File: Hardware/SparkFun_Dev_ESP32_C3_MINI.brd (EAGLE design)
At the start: 17.8 x 33 mm, 44 parts, among them J1 USB Female Type C Connector, J5 Vertical Qwiic Connector, U2 RT9080-33GJ5

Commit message: Some updates to layout
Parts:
- moved U$1 5.46 mm to (10.2, 11.2)
- moved J5 4.57 mm to (10.2, 21.1)
- moved C8 3.81 mm to (17.8, 6.35)
- moved C9 3.43 mm to (17.8, 7.24)
- moved R3 2.54 mm to (15.2, 17.8)
- moved R4 2.54 mm to (5.08, 17.8)
- moved C1 2.54 mm to (12.7, 24.1)
- moved C2 2.54 mm to (12.7, 22.9)
- moved C5 2.54 mm to (7.62, 22.9)
- moved R11 2.54 mm to (7.62, 24.1)
- moved R5 2.54 mm to (7.62, 25.4)
- moved R6 2.54 mm to (12.7, 25.4)
- moved U2 1.65 mm to (10.2, 23.2)
- moved BOOT 1.27 mm to (15.2, 22.9)
- moved R7 1.27 mm to (5.08, 19.1)
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
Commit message: Removes unnecessary documents, , moves boar daround
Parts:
- moved PWR 16.7 mm to (6.22, 15.2)
- moved STAT 16.7 mm to (14.6, 15.2)
- moved FD3 15.3 mm to (2.54, 6.35)
- moved FD4 15.3 mm to (2.54, 6.35)
- moved LOGO2 12.3 mm to (14.2, 18.5), turned to 90 degrees
- moved FD1 10.2 mm to (16.5, 26.7), flipped to the bottom
- moved FD2 10.2 mm to (16.5, 26.7), flipped to the top
- moved SHLD 5.36 mm to (14.7, 29.8), turned to 0 degrees
- moved R9 1.27 mm to (16.5, 19.1), turned to 90 degrees
- moved TP1 1.27 mm to (15.2, 12.7)
- moved TP6 1.27 mm to (12.7, 12.7)
- moved TP3 1.27 mm to (15.2, 7.62)
- moved TP4 1.27 mm to (12.7, 7.62)
- moved R3 1.27 mm to (15.2, 19.1), turned to 90 degrees
- moved TP2 1.27 mm to (15.2, 10.2)
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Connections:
- net IO10: now also U$2.2, U$2.2B; no longer U$2.1, U$2.1B
- net IO8: now also U$2.1, U$2.1B; no longer U$2.2, U$2.2B
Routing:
- added copper zone on layer 15, net 3V3
- added copper zone on layer 1, net GND
- added copper zone on layer 16, net GND
- added copper zone on layer 2, net GND

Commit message: Fixes net names that were blasted away
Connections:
- removed net IO7/STAT: STAT.2, TP1.1, U$1.21, U$2.3, U$2.3B
- removed net IOA0/SCLK: U$1.12, U$3.7, U$3.7B
- removed net IOA1/POCI: U$1.13, U$3.6, U$3.6B
- removed net IOA3/PICO: TP4.1, U$1.6, U$3.5, U$3.5B
- removed net IOA4: U$1.18, U$3.8, U$3.8B
- new net IO7: U$1.21, U$2.3, U$2.3B
- new net IOA0/SCLK/MTCK: TP3.1, U$1.12, U$3.7, U$3.7B
- new net IOA1/POCI/MTDO: STAT.2, TP1.1, U$1.13, U$3.6, U$3.6B
- new net IOA3/PICO/MTDI: TP6.1, U$1.6, U$3.5, U$3.5B
- new net IOA4/MTMS: TP4.1, U$1.18, U$3.8, U$3.8B
- net IO5/SCL: no longer TP6.1
- net IO6/SDA: no longer TP3.1
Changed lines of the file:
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@@
 <wire x1="19.35" y1="8.89" x2="17.78" y2="8.89" width="0" layer="19" extent="1-1"/>
 </signal>
-<signal name="IO7/STAT">
-<contactref element="TP1" pad="1"/>
-<contactref element="U$1" pad="21"/>
-<contactref element="STAT" pad="2"/>
-<contactref element="U$2" pad="3B"/>
-<contactref element="U$2" pad="3"/>
-<wire x1="15.1257" y1="15.24" x2="15.24" y2="12.7" width="0" layer="19" extent="16-16"/>
-<wire x1="7.76" y1="16.076" x2="15.1257" y2="15.24" width="0" layer="19" extent="1-16"/>
-<wire x1="2.54" y1="13.97" x2="7.76" y2="16.076" width="0" layer="19" extent="1-1"/>
-<wire x1="0.97" y1="13.97" x2="2.54" y2="13.97" width="0" layer="19" extent="1-1"/>
-</signal>
-<signal name="IOA3/PICO">
-<contactref element="TP4" pad="1"/>
+<signal name="IOA3/PICO/MTDI">
 <contactref element="U$1" pad="6"/>
 <contactref element="U$3" pad="5"/>
 <contactref element="U$3" pad="5B"/>
+<contactref element="TP6" pad="1"/>
 <wire x1="19.35" y1="19.05" x2="17.78" y2="19.05" width="0" layer="19" extent="1-1"/>
 <wire x1="16.06" y1="11.176" x2="17.78" y2="19.05" width="0" layer="19" extent="1-1"/>
-<wire x1="12.7" y1="7.62" x2="16.06" y2="11.176" width="0" layer="19" extent="1-16"/>
+<wire x1="12.7" y1="12.7" x2="16.06" y2="11.176" width="0" layer="19" extent="1-16"/>
 </signal>
-<signal name="IOA1/POCI">
+<signal name="IOA1/POCI/MTDO">
 <contactref element="U$1" pad="13"/>
 <contactref element="U$3" pad="6"/>
 <contactref element="U$3" pad="6B"/>
+<contactref element="TP1" pad="1"/>
+<contactref element="STAT" pad="2"/>
 <wire x1="19.35" y1="16.51" x2="17.78" y2="16.51" width="0" layer="19" extent="1-1"/>
-<wire x1="14.16" y1="16.076" x2="17.78" y2="16.51" width="0" layer="19" extent="1-1"/>
+<wire x1="15.1257" y1="15.24" x2="17.78" y2="16.51" width="0" layer="19" extent="16-16"/>
+<wire x1="14.16" y1="16.076" x2="15.1257" y2="15.24" width="0" layer="19" extent="1-16"/>
+<wire x1="15.24" y1="12.7" x2="15.1257" y2="15.24" width="0" layer="19" extent="16-16"/>
 </signal>
-<signal name="IOA0/SCLK">
+<signal name="IOA0/SCLK/MTCK">
 <contactref element="U$1" pad="12"/>
 <contactref element="U$3" pad="7B"/>
 <contactref element="U$3" pad="7"/>
+<contactref element="TP3" pad="1"/>
 <wire x1="17.78" y1="13.97" x2="19.35" y2="13.97" width="0" layer="19" extent="1-1"/>
 <wire x1="14.96" y1="16.076" x2="17.78" y2="13.97" width="0" layer="19" extent="1-1"/>
+<wire x1="15.24" y1="7.62" x2="17.78" y2="13.97" width="0" layer="19" extent="16-16"/>
 </signal>
 <signal name="N$3">
@@
 <wire x1="6.16" y1="16.076" x2="14.44" y2="20.81" width="0" layer="19" extent="1-1"/>
 </signal>
-<signal name="IOA4">
+<signal name="IOA4/MTMS">
 <contactref element="U$1" pad="18"/>
 <contactref element="U$3" pad="8B"/>
 <contactref element="U$3" pad="8"/>
+<contactref element="TP4" pad="1"/>
 <wire x1="17.78" y1="11.43" x2="19.35" y2="11.43" width="0" layer="19" extent="1-1"/>
-<wire x1="10.16" y1="16.076" x2="17.78" y2="11.43" width="0" layer="19" extent="1-1"/>
+<wire x1="12.7" y1="7.62" x2="17.78" y2="11.43" width="0" layer="19" extent="16-16"/>
+<wire x1="10.16" y1="16.076" x2="12.7" y2="7.62" width="0" layer="19" extent="1-16"/>
 </signal>
 <signal name="IO5/SCL">
 <contactref element="J5" pad="4"/>
-<contactref element="TP6" pad="1"/>
 <contactref element="U$1" pad="19"/>
 <contactref element="R4" pad="2"/>
@@
 <wire x1="0.97" y1="19.05" x2="2.54" y2="19.05" width="0" layer="19" extent="1-1"/>
 <wire x1="9.36" y1="16.076" x2="5.58" y2="17.78" width="0" layer="19" extent="1-1"/>
-<wire x1="12.7" y1="12.7" x2="9.36" y2="16.076" width="0" layer="19" extent="1-16"/>
 </signal>
 <signal name="IO6/SDA">
 <contactref element="J5" pad="3"/>
-<contactref element="TP3" pad="1"/>
 <contactref element="U$1" pad="20"/>
 <contactref element="R3" pad="1"/>
@@
 <wire x1="2.54" y1="16.51" x2="8.56" y2="16.076" width="0" layer="19" extent="1-1"/>
 <wire x1="0.97" y1="16.51" x2="2.54" y2="16.51" width="0" layer="19" extent="1-1"/>
-<wire x1="15.24" y1="7.62" x2="8.56" y2="16.076" width="0" layer="19" extent="1-16"/>
 </signal>
 <signal name="3V3">
@@
 </polygon>
 </signal>
+<signal name="IO7">
+<contactref element="U$2" pad="3B"/>
+<contactref element="U$2" pad="3"/>
+<contactref element="U$1" pad="21"/>
+<wire x1="2.54" y1="13.97" x2="7.76" y2="16.076" width="0" layer="19" extent="1-1"/>
+<wire x1="0.97" y1="13.97" x2="2.54" y2="13.97" width="0" layer="19" extent="1-1"/>
+</signal>
 </signals>

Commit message: Adds I2S nets, we'll see
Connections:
- net IO10 renamed IO10/I2S_WS
- net IO5/SCL renamed IO5/SCL/BCK
- net IO6/SDA renamed IO6/SDA/I2S_SDO
- net IO7 renamed IO7/I2S_SDI
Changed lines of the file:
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@@
 <layers>
 <layer number="1" name="Top" color="4" fill="1" visible="yes" active="yes"/>
-<layer number="2" name="Route2" color="23" fill="1" visible="yes" active="yes"/>
-<layer number="15" name="Route15" color="10" fill="1" visible="yes" active="yes"/>
+<layer number="2" name="Route2" color="23" fill="1" visible="no" active="yes"/>
+<layer number="15" name="Route15" color="10" fill="1" visible="no" active="yes"/>
 <layer number="16" name="Bottom" color="3" fill="1" visible="yes" active="yes"/>
 <layer number="17" name="Pads" color="26" fill="1" visible="yes" active="yes"/>
@@
 <layer number="19" name="Unrouted" color="6" fill="1" visible="yes" active="yes"/>
 <layer number="20" name="Dimension" color="15" fill="1" visible="yes" active="yes"/>
-<layer number="21" name="tPlace" color="16" fill="1" visible="no" active="yes"/>
-<layer number="22" name="bPlace" color="14" fill="1" visible="no" active="yes"/>
+<layer number="21" name="tPlace" color="16" fill="1" visible="yes" active="yes"/>
+<layer number="22" name="bPlace" color="14" fill="1" visible="yes" active="yes"/>
 <layer number="23" name="tOrigins" color="15" fill="1" visible="yes" active="yes"/>
 <layer number="24" name="bOrigins" color="15" fill="1" visible="yes" active="yes"/>
@@
 <layer number="37" name="tTest" color="7" fill="1" visible="no" active="yes"/>
 <layer number="38" name="bTest" color="7" fill="1" visible="no" active="yes"/>
-<layer number="39" name="tKeepout" color="4" fill="11" visible="yes" active="yes"/>
+<layer number="39" name="tKeepout" color="4" fill="11" visible="no" active="yes"/>
 <layer number="40" name="bKeepout" color="1" fill="11" visible="no" active="yes"/>
 <layer number="41" name="tRestrict" color="4" fill="10" visible="no" active="yes"/>
@@
 <wire x1="14.0843" y1="15.24" x2="18.264" y2="31.75" width="0" layer="19" extent="1-16"/>
 </signal>
-<signal name="IO10">
+<signal name="IO10/I2S_WS">
 <contactref element="U$1" pad="16"/>
 <contactref element="U$2" pad="2B"/>
@@
 <wire x1="10.16" y1="16.076" x2="12.7" y2="7.62" width="0" layer="19" extent="1-16"/>
 </signal>
-<signal name="IO5/SCL">
+<signal name="IO5/SCL/BCK">
 <contactref element="J5" pad="4"/>
 <contactref element="U$1" pad="19"/>
@@
 <wire x1="9.36" y1="16.076" x2="5.58" y2="17.78" width="0" layer="19" extent="1-1"/>
 </signal>
-<signal name="IO6/SDA">
+<signal name="IO6/SDA/I2S_SDO">
 <contactref element="J5" pad="3"/>
 <contactref element="U$1" pad="20"/>
@@
 </polygon>
 </signal>
-<signal name="IO7">
+<signal name="IO7/I2S_SDI">
 <contactref element="U$2" pad="3B"/>
 <contactref element="U$2" pad="3"/>

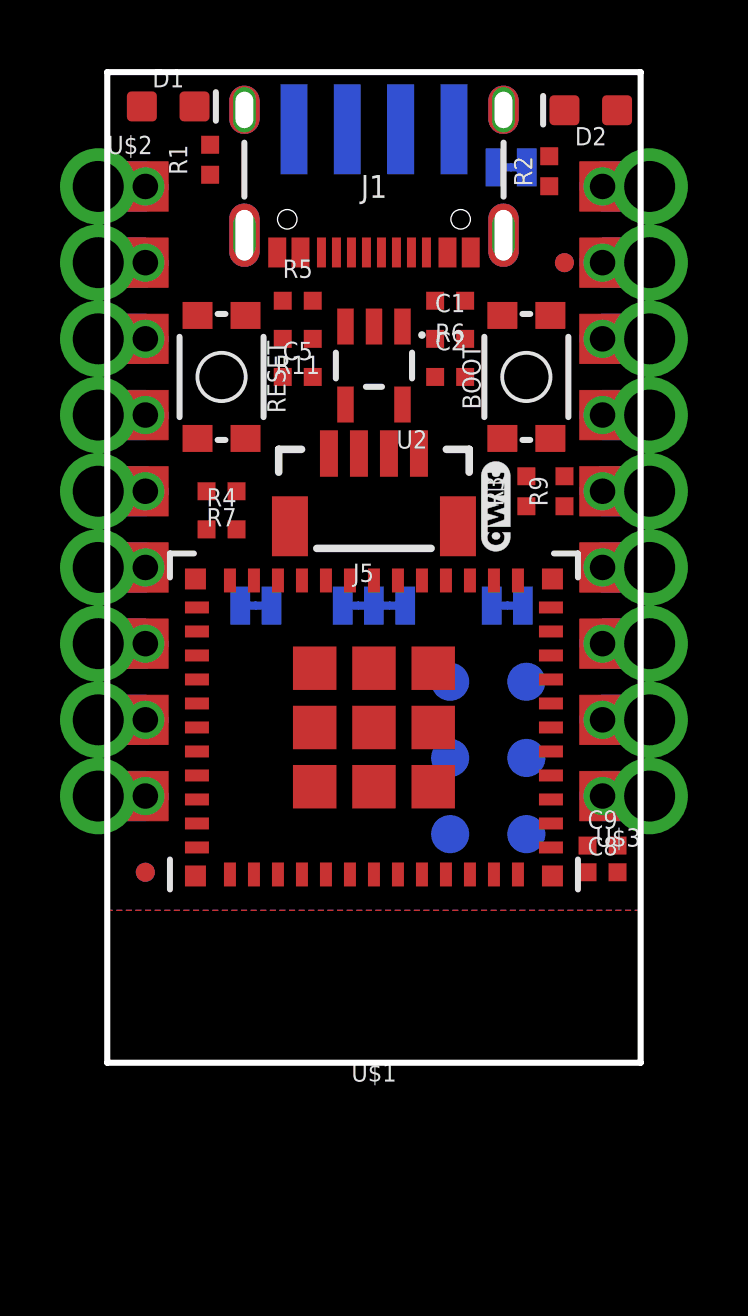
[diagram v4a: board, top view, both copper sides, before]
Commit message: Adds new C3 module so that the  device value is correct
* Fixes testpoints
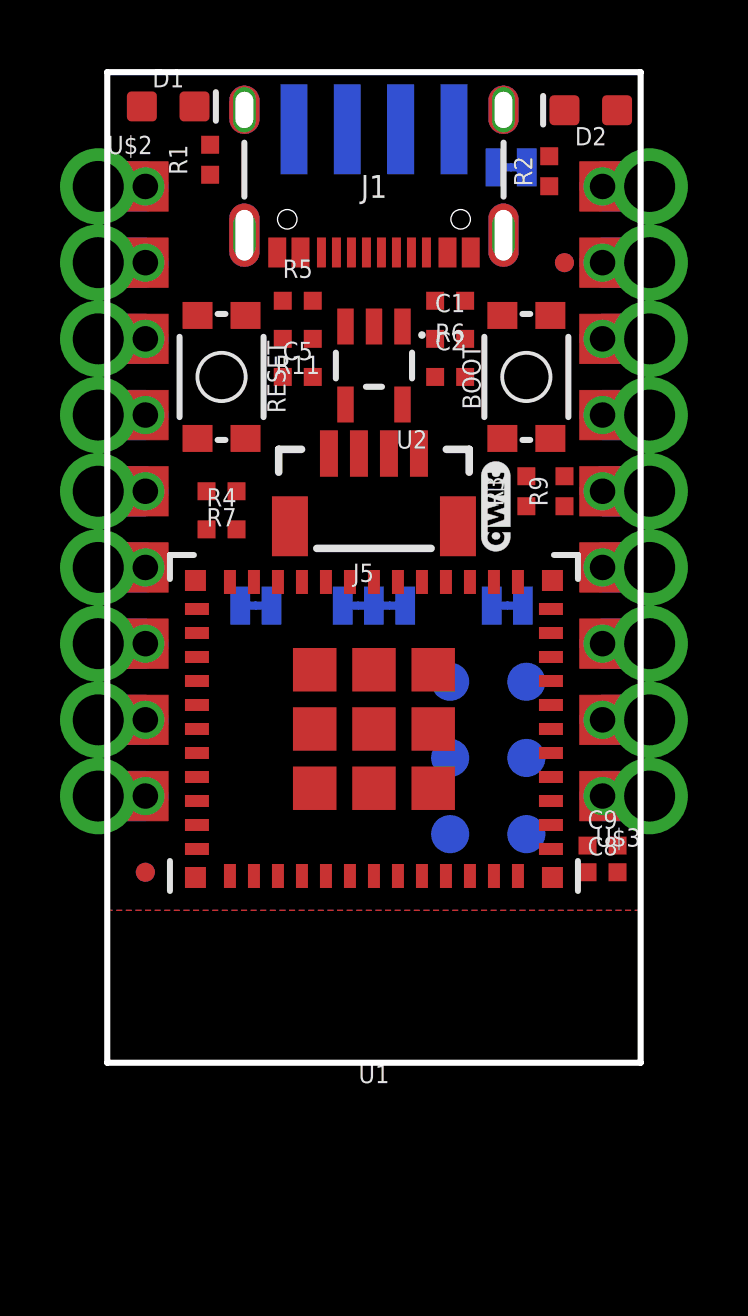
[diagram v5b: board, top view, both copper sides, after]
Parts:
- removed U$1: ESP32-C3_MINI-1, ESP32-C3-MINI-1:ESP32-C3-MINI-1
- added U1: ESP32-C3_MINI-1, ESP32-C3-MINI-1:ESP32-C3-MINI-1
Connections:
- removed net IOA1/POCI/MTDO: STAT.2, TP1.1, U$1.13, U$3.6, U$3.6B
- removed net IOA3/PICO/MTDI: TP6.1, U$1.6, U$3.5, U$3.5B
- new net IOA1/POCI/MTDI: STAT.2, TP6.1, U$3.6, U$3.6B, U1.13
- new net IOA3/PICO/MTDO: TP1.1, U$3.5, U$3.5B, U1.6
- net 3.3V: now also U1.3; no longer U$1.3
- net EN: now also U1.8; no longer U$1.8
- net GND: now also U1.1, U1.11, U1.14, U1.2, U1.36, U1.37, U1.38, U1.39, U1.40, U1.41, U1.42, U1.43, U1.44, U1.45, U1.46, U1.47, U1.48, U1.49.1, U1.49.2, U1.49.3, U1.49.4, U1.49.5, U1.49.6, U1.49.7, U1.49.8, U1.49.9, U1.50, U1.51, U1.52, U1.53; no longer U$1.1, U$1.11, U$1.14, U$1.2, U$1.36, U$1.37, U$1.38, U$1.39, U$1.40, U$1.41, U$1.42, U$1.43, U$1.44, U$1.45, U$1.46, U$1.47, U$1.48, U$1.49.1, U$1.49.2, U$1.49.3, U$1.49.4, U$1.49.5, U$1.49.6, U$1.49.7, U$1.49.8, U$1.49.9, U$1.50, U$1.51, U$1.52, U$1.53
- net IO10/I2S_WS: now also U1.16; no longer U$1.16
- net IO18/USB_N: now also U1.26; no longer U$1.26
- net IO19/USB_P: now also U1.27; no longer U$1.27
- net IO20/TXO: now also U1.30; no longer U$1.30
- net IO21/RXI: now also U1.31; no longer U$1.31
- net IO5/SCL/BCK: now also U1.19; no longer U$1.19
- net IO6/SDA/I2S_SDO: now also U1.20; no longer U$1.20
- net IO7/I2S_SDI: now also U1.21; no longer U$1.21
- net IO8: now also U1.22; no longer U$1.22
- net IO9/BOOT: now also U1.23; no longer U$1.23
- net IOA0/SCLK/MTCK: now also U1.12; no longer U$1.12
- net IOA2: now also U1.5; no longer U$1.5
- net IOA4/MTMS: now also U1.18; no longer U$1.18

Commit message: Moves stat LED
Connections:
- net IO10/I2S_WS: now also STAT.2
- net IOA1/POCI/MTDI: no longer STAT.2
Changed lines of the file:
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@@
 <contactref element="U$3" pad="6"/>
 <contactref element="U$3" pad="6B"/>
-<contactref element="STAT" pad="2"/>
 <contactref element="TP6" pad="1"/>
 <contactref element="U1" pad="13"/>
+<wire x1="19.35" y1="16.51" x2="17.78" y2="16.51" width="0" layer="19" extent="1-1"/>
+<wire x1="14.16" y1="16.0252" x2="17.78" y2="16.51" width="0" layer="19" extent="1-1"/>
 <wire x1="12.7" y1="12.7" x2="14.16" y2="16.0252" width="0" layer="19" extent="1-16"/>
-<wire x1="15.1257" y1="15.24" x2="12.7" y2="12.7" width="0" layer="19" extent="16-16"/>
-<wire x1="17.78" y1="16.51" x2="15.1257" y2="15.24" width="0" layer="19" extent="16-16"/>
-<wire x1="19.35" y1="16.51" x2="17.78" y2="16.51" width="0" layer="19" extent="1-1"/>
 </signal>
 <signal name="IOA0/SCLK/MTCK">
@@
 <contactref element="U$2" pad="2"/>
 <contactref element="U1" pad="16"/>
-<wire x1="0.97" y1="11.43" x2="11.76" y2="16.0252" width="0" layer="19" extent="1-1"/>
-<wire x1="2.54" y1="11.43" x2="0.97" y2="11.43" width="0" layer="19" extent="1-1"/>
+<contactref element="STAT" pad="2"/>
+<wire x1="11.76" y1="16.0252" x2="15.1257" y2="15.24" width="0" layer="19" extent="1-16"/>
+<wire x1="2.54" y1="11.43" x2="11.76" y2="16.0252" width="0" layer="19" extent="1-1"/>
+<wire x1="0.97" y1="11.43" x2="2.54" y2="11.43" width="0" layer="19" extent="1-1"/>
 </signal>
 <signal name="IO9/BOOT">

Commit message: Paranoid upload
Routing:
- net V_USB: track 0.00 -> 2.02 mm, vias 0 -> 2
- added copper zone on layer 2, net V_USB

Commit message: Routes some nets
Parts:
- moved I2C 3.17 mm to (10.2, 18.4)
- moved PWR 2.95 mm to (9.14, 14.9)
- moved STAT 2.82 mm to (11.8, 14.9)
- moved R4 1.27 mm to (5.08, 19.1)
- moved R7 1.27 mm to (5.08, 17.8)
- moved SHLD 0.13 mm to (14.6, 29.8), turned to 180 degrees
- turned R11 to 0 degrees
- turned R3 to 270 degrees
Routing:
- net IO19/USB_P: track 0.00 -> 28.5 mm, vias 0 -> 2
- net IO18/USB_N: track 0.00 -> 25.2 mm, vias 0 -> 2
- net 3.3V: track 0.00 -> 14.6 mm, vias 0 -> 4
- net V_USB: track 2.02 -> 8.91 mm, vias 2 -> 4
- net EN: track 0.00 -> 5.70 mm
- net IO6/SDA/I2S_SDO: track 0.00 -> 4.74 mm
- net IO9/BOOT: track 0.00 -> 4.10 mm
- net N$8: track 0.00 -> 1.94 mm
- net N$3: track 0.00 -> 1.74 mm
- net N$7: track 0.00 -> 1.73 mm
- net N$1: track 0.00 -> 1.49 mm
- net GND: track 0.00 -> 1.16 mm, vias 0 -> 2
- added copper zone on layer 15, net 3.3V
- removed copper zone on layer 15, net 3V3
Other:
- board text added: "1"
- board text added: "4"
